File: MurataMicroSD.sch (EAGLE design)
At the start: 14 parts, among them CON1 CON_TC2030-CTL-NL, U1 IC_BLE_LBCA2HNZYZ-711

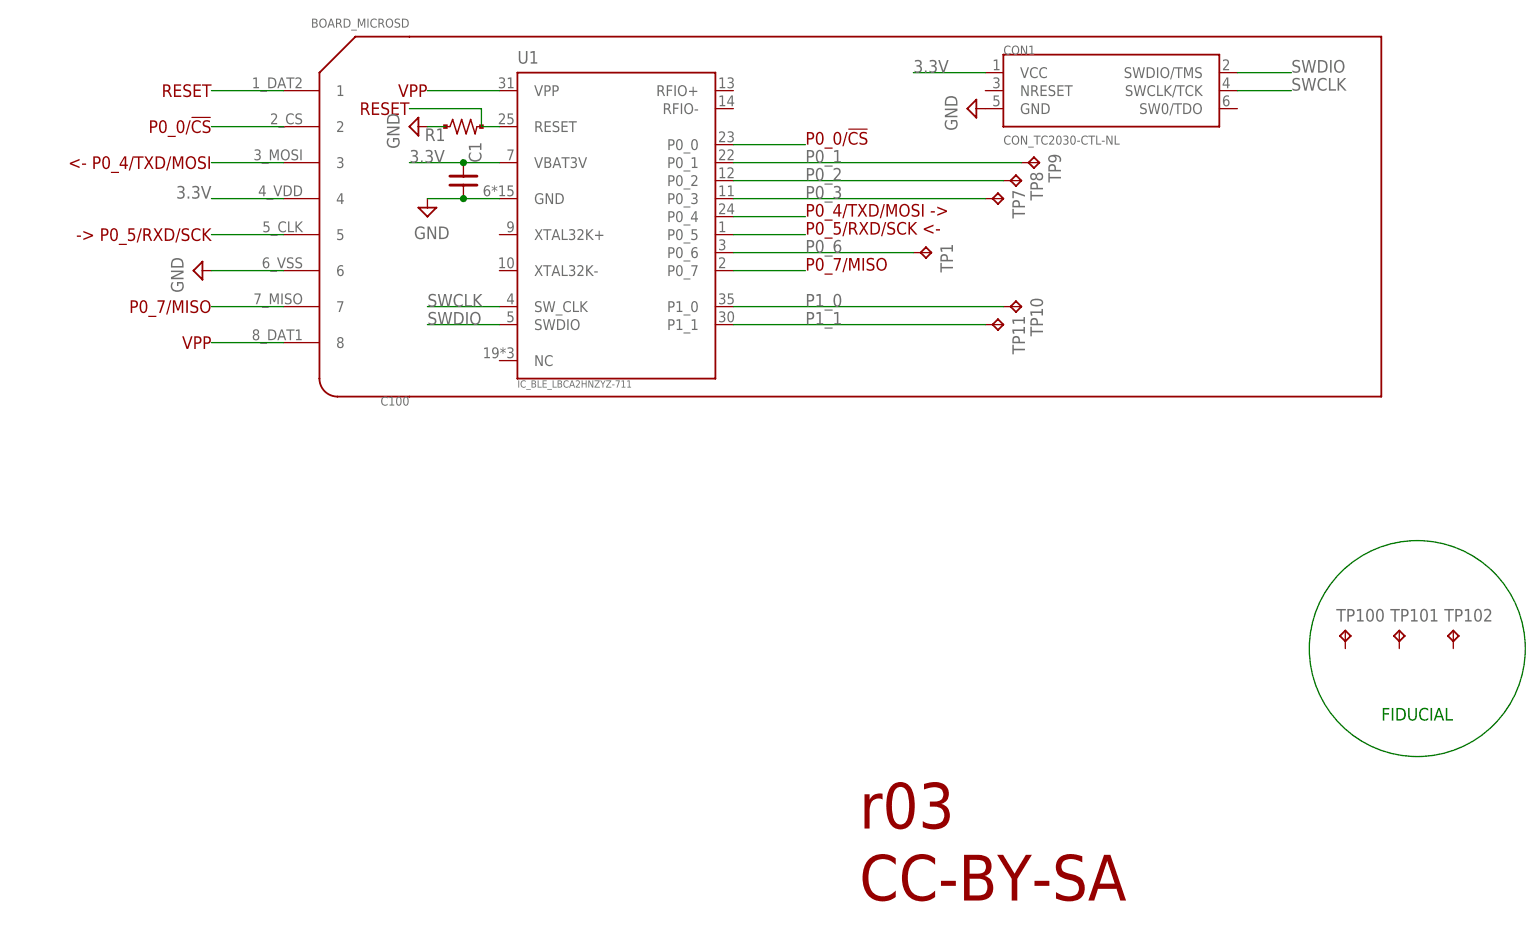
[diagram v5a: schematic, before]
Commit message: [ FIX ] add SPI ROM; board size extend; silk move
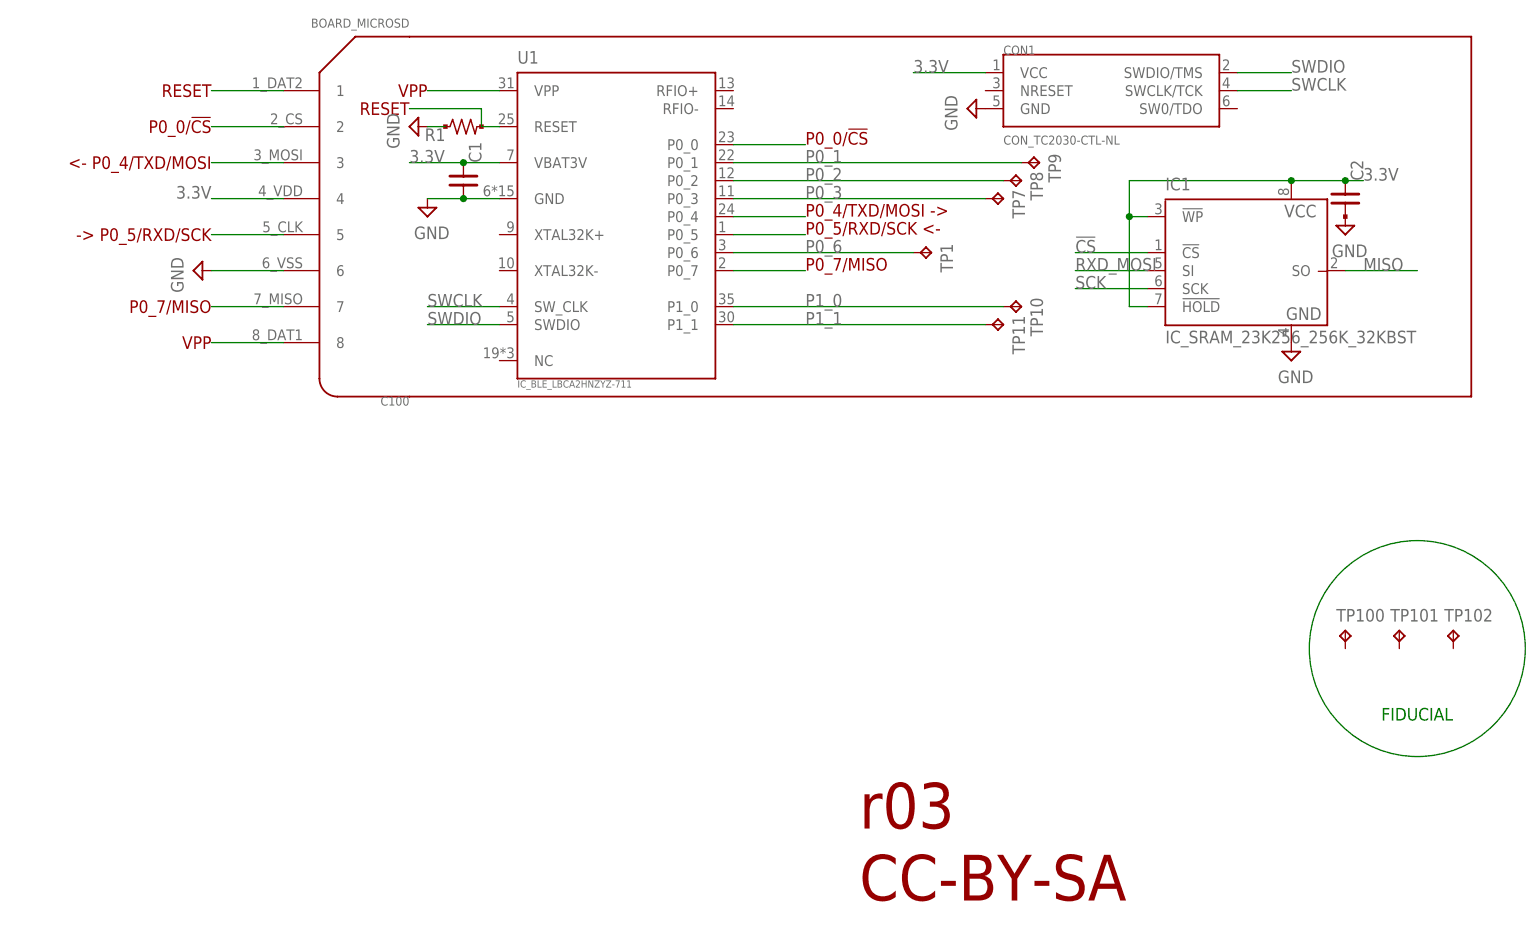
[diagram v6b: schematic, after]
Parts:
- added C2: (no value), mylib:C_PAD_PAD_1005
- added IC1: IC_SRAM_23K256_256K_32KBST, mylib:IC_SRAM_23K256_256K_32KBST
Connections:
- net !CS!: now also IC1.!CS
- net 3.3V: now also C2.1, IC1.!HOLD, IC1.!WP, IC1.VCC
- net GND: now also C2.2, IC1.GND
- net MISO: now also IC1.SO
- net RXD_MOSI: now also IC1.SI
- net SCK: now also IC1.SCK
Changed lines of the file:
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@@
 <part name="SUPPLY4" library="mylib" deviceset="GND" device=""/>
 <part name="TP1" library="testpad_local" deviceset="TP" device="TP08R"/>
+<part name="IC1" library="mylib" deviceset="IC_SRAM_23K256_256K_32KB" device="ST"/>
+<part name="SUPPLY5" library="mylib" deviceset="GND" device=""/>
+<part name="C2" library="mylib" deviceset="C_PAD_PAD_" device="1005"/>
+<part name="SUPPLY6" library="mylib" deviceset="GND" device=""/>
 </parts>
 <sheets>
@@
 <text x="71.12" y="99.06" size="1.778" layer="94" rot="MR0" align="center-left">-&gt; P0_5/RXD/SCK</text>
 <text x="71.12" y="109.22" size="1.778" layer="94" rot="MR0" align="center-left">&lt;- P0_4/TXD/MOSI</text>
-<wire x1="99.06" y1="76.2" x2="236.22" y2="76.2" width="0.254" layer="94"/>
-<wire x1="236.22" y1="76.2" x2="236.22" y2="127" width="0.254" layer="94"/>
-<wire x1="236.22" y1="127" x2="99.06" y2="127" width="0.254" layer="94"/>
+<wire x1="99.06" y1="76.2" x2="248.92" y2="76.2" width="0.254" layer="94"/>
+<wire x1="248.92" y1="76.2" x2="248.92" y2="127" width="0.254" layer="94"/>
+<wire x1="248.92" y1="127" x2="99.06" y2="127" width="0.254" layer="94"/>
 <text x="71.12" y="88.9" size="1.778" layer="94" rot="MR0" align="center-left">P0_7/MISO</text>
 <text x="154.94" y="93.98" size="1.778" layer="94">P0_7/MISO</text>
@@
 <instance part="SUPPLY4" gate="GND" x="177.8" y="116.84" rot="R270"/>
 <instance part="TP1" gate="G$1" x="172.72" y="96.52" rot="R270"/>
+<instance part="IC1" gate="G$1" x="218.44" y="93.98"/>
+<instance part="SUPPLY5" gate="GND" x="223.52" y="81.28"/>
+<instance part="C2" gate="G$1" x="231.14" y="104.14"/>
+<instance part="SUPPLY6" gate="GND" x="231.14" y="99.06"/>
 </instances>
 <busses>
@@
 <label x="170.18" y="121.92" size="1.778" layer="95"/>
 </segment>
+<segment>
+<wire x1="233.68" y1="106.68" x2="231.14" y2="106.68" width="0.1524" layer="91"/>
+<pinref part="IC1" gate="G$1" pin="VCC"/>
+<wire x1="231.14" y1="106.68" x2="223.52" y2="106.68" width="0.1524" layer="91"/>
+<wire x1="223.52" y1="106.68" x2="200.66" y2="106.68" width="0.1524" layer="91"/>
+<junction x="223.52" y="106.68"/>
+<wire x1="200.66" y1="106.68" x2="200.66" y2="101.6" width="0.1524" layer="91"/>
+<pinref part="IC1" gate="G$1" pin="!WP"/>
+<wire x1="200.66" y1="101.6" x2="203.2" y2="101.6" width="0.1524" layer="91"/>
+<pinref part="IC1" gate="G$1" pin="!HOLD"/>
+<wire x1="203.2" y1="88.9" x2="200.66" y2="88.9" width="0.1524" layer="91"/>
+<wire x1="200.66" y1="88.9" x2="200.66" y2="101.6" width="0.1524" layer="91"/>
+<junction x="200.66" y="101.6"/>
+<label x="233.68" y="106.68" size="1.778" layer="95"/>
+<pinref part="C2" gate="G$1" pin="1"/>
+<junction x="231.14" y="106.68"/>
+</segment>
 </net>
 <net name="GND" class="0">
@@
 <pinref part="SUPPLY4" gate="GND" pin="GND"/>
 </segment>
+<segment>
+<pinref part="IC1" gate="G$1" pin="GND"/>
+<pinref part="SUPPLY5" gate="GND" pin="GND"/>
+</segment>
+<segment>
+<pinref part="C2" gate="G$1" pin="2"/>
+<pinref part="SUPPLY6" gate="GND" pin="GND"/>
+</segment>
 </net>
 <net name="N$1" class="0">
@@
 <pinref part="U1" gate="G$1" pin="P0_7"/>
 </segment>
+<segment>
+<wire x1="241.3" y1="93.98" x2="231.14" y2="93.98" width="0.1524" layer="91"/>
+<label x="233.68" y="93.98" size="1.778" layer="95"/>
+<pinref part="IC1" gate="G$1" pin="SO"/>
+</segment>
 </net>
 <net name="P0_6" class="0">
@@
 <pinref part="U1" gate="G$1" pin="P0_4"/>
 </segment>
+<segment>
+<wire x1="203.2" y1="93.98" x2="193.04" y2="93.98" width="0.1524" layer="91"/>
+<label x="193.04" y="93.98" size="1.778" layer="95"/>
+<pinref part="IC1" gate="G$1" pin="SI"/>
+</segment>
 </net>
 <net name="!CS!" class="0">
@@
 <wire x1="154.94" y1="111.76" x2="144.78" y2="111.76" width="0.1524" layer="91"/>
 <pinref part="U1" gate="G$1" pin="P0_0"/>
+</segment>
+<segment>
+<wire x1="203.2" y1="96.52" x2="193.04" y2="96.52" width="0.1524" layer="91"/>
+<label x="193.04" y="96.52" size="1.778" layer="95"/>
+<pinref part="IC1" gate="G$1" pin="!CS"/>
 </segment>
 </net>
@@
 <pinref part="U1" gate="G$1" pin="P0_5"/>
 </segment>
-</net>
+<segment>
+<wire x1="203.2" y1="91.44" x2="193.04" y2="91.44" width="0.1524" layer="91"/>
+<label x="193.04" y="91.44" size="1.778" layer="95"/>
+<pinref part="IC1" gate="G$1" pin="SCK"/>
+</segment>
+</net>

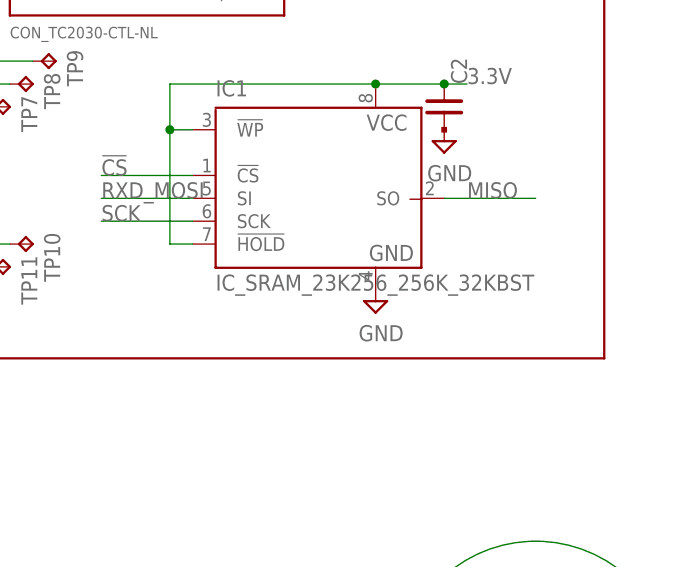
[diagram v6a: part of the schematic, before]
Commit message: [ uSD ] move silk; tiny trace fix
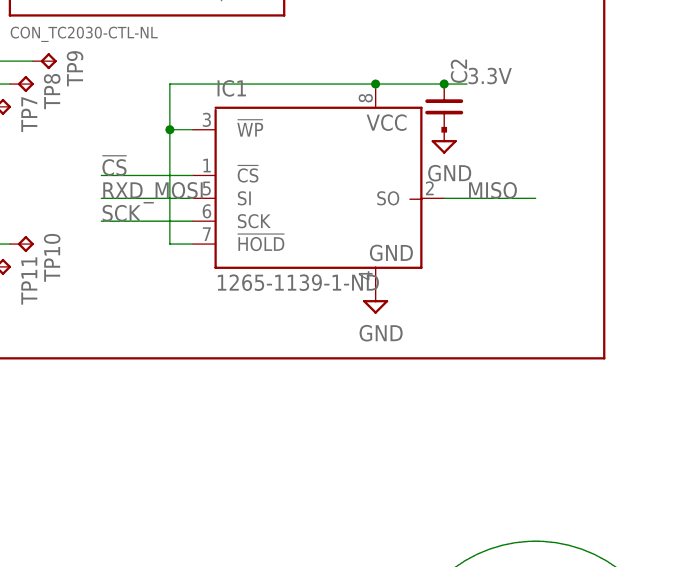
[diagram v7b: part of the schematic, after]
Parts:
- IC1: value IC_SRAM_23K256_256K_32KBST -> 1265-1139-1-ND
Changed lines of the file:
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@@
 <part name="SUPPLY4" library="mylib" deviceset="GND" device=""/>
 <part name="TP1" library="testpad_local" deviceset="TP" device="TP08R"/>
-<part name="IC1" library="mylib" deviceset="IC_SRAM_23K256_256K_32KB" device="ST"/>
+<part name="IC1" library="mylib" deviceset="IC_SRAM_23K256_256K_32KB" device="ST" value="1265-1139-1-ND"/>
 <part name="SUPPLY5" library="mylib" deviceset="GND" device=""/>
 <part name="C2" library="mylib" deviceset="C_PAD_PAD_" device="1005"/>

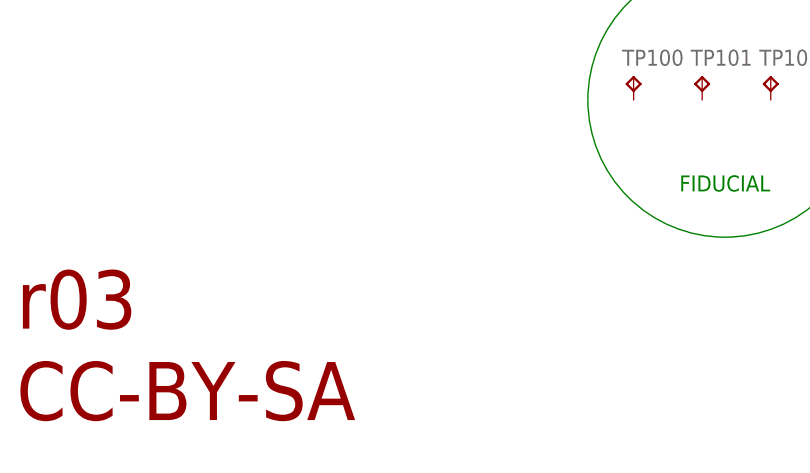
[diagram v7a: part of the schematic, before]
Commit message: [ uSD ] OSHW icon replaced from library
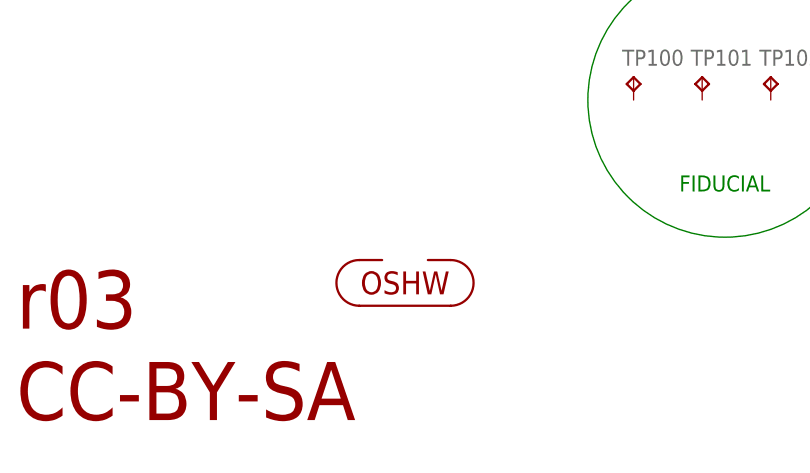
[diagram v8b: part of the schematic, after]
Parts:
- added U$1: ICON_OSHW, mylib:ICON_OSHW
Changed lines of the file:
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@@
 <part name="C2" library="mylib" deviceset="C_PAD_PAD_" device="1005"/>
 <part name="SUPPLY6" library="mylib" deviceset="GND" device=""/>
+<part name="U$1" library="mylib" deviceset="ICON_OSHW" device=""/>
 </parts>
 <sheets>
@@
 <instance part="C2" gate="G$1" x="231.14" y="104.14"/>
 <instance part="SUPPLY6" gate="GND" x="231.14" y="99.06"/>
+<instance part="U$1" gate="G$1" x="205.74" y="20.32"/>
 </instances>
 <busses>
